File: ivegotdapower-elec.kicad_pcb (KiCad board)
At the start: 2 copper layers, 87 x 70 mm, 74 parts, among them J1 Conn_Debug, J10 Conn_+3.3V, J11 Conn_bau, J12 CAN_conn, J13 CAN_conn, J2 Conn_batt, J3 Conn_alim, J4 Conn_TSMR, J5 Conn_POW2, J6 Conn_POW1, J7 Conn_RPi, J8 Conn_+5V, Q1 IRFR5305, Q2 IRFR5305, Q3 BSS138, Q4 MMBT2907A, Q5 MMBT2907A, Q6 MMBT2907A, Q7 MMBT2907A, U1 TCAN332, U10 LD1117S33TR_SOT223, U11 LM358, U6 ACS711xLCTR-12AB, U7 STM32F303K8Tx, U8 LD1117S50TR_SOT223

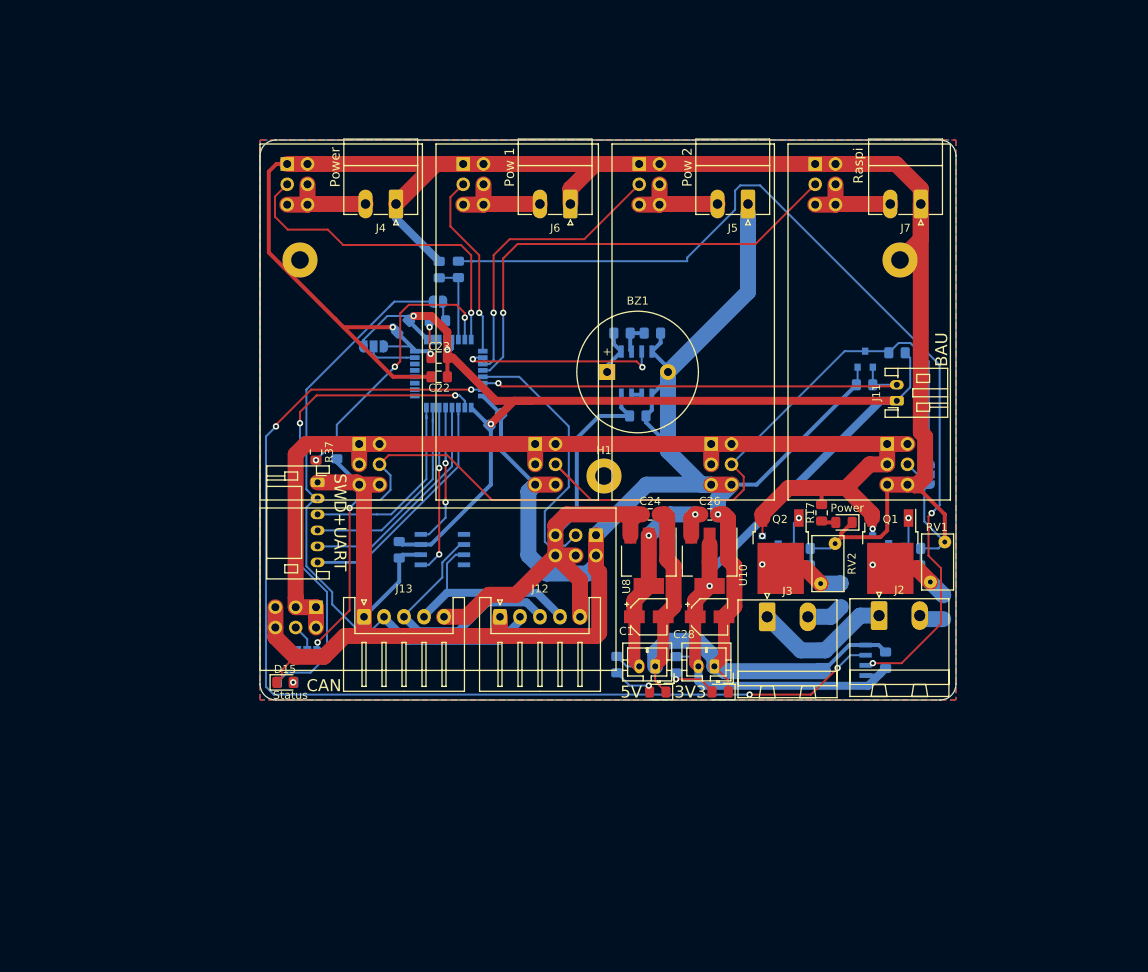
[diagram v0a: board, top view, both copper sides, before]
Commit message: Refactoring. Add protection (OpAmps) on analog measures
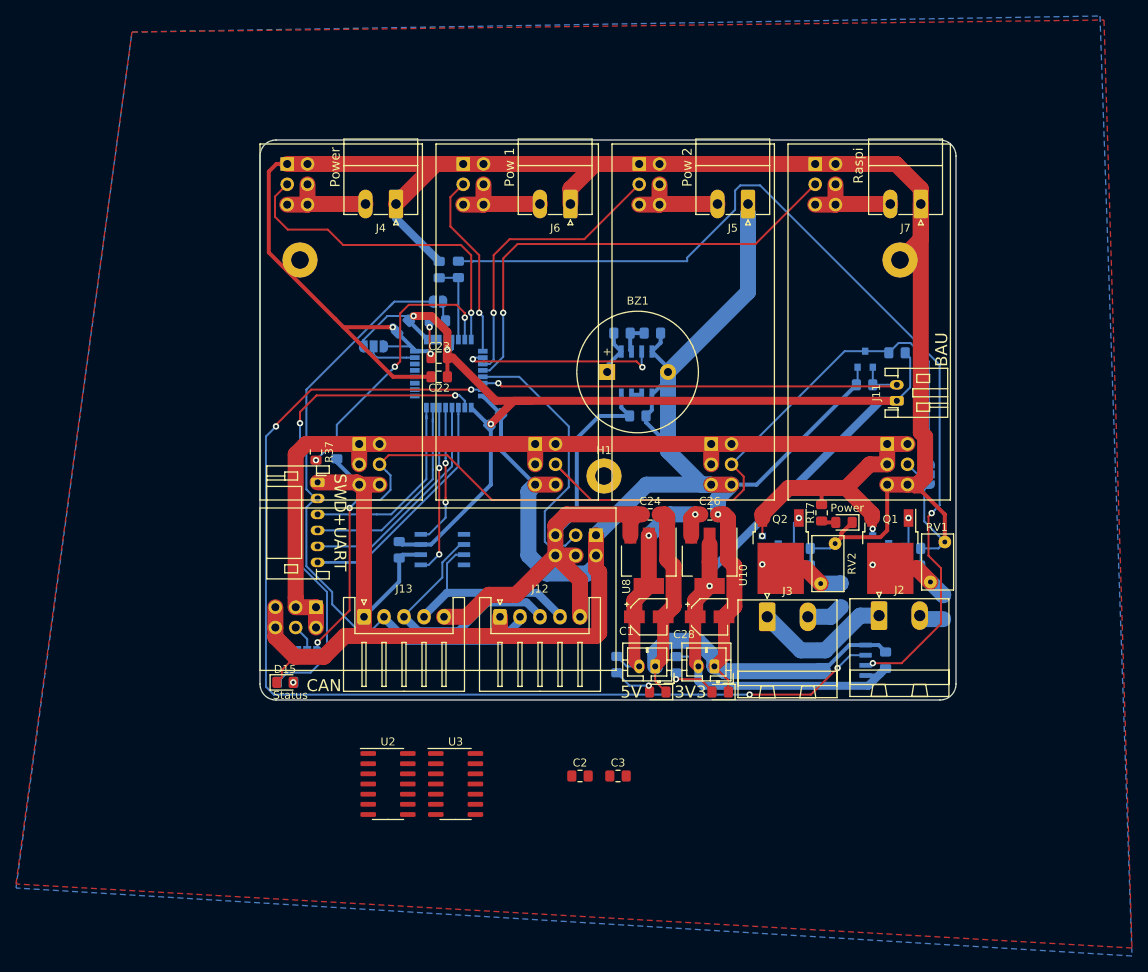
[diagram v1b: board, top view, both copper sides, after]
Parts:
- added C2: 100nF, Capacitor_SMD:C_0805_2012Metric_Pad1.15x1.40mm_HandSolder, F.Cu at (120.0, 129.5)
- added C3: 100nF, Capacitor_SMD:C_0805_2012Metric_Pad1.15x1.40mm_HandSolder, F.Cu at (124.8, 129.5)
- added U2: LM324, Package_SO:SOIC-14_3.9x8.7mm_P1.27mm, F.Cu at (96.0, 130.5)
- added U3: LM324, Package_SO:SOIC-14_3.9x8.7mm_P1.27mm, F.Cu at (104.5, 130.5)
- R37: value R -> 75k
- R38: value R -> 15k
- U10: value LD1117S33TR_SOT223 -> LD1117S33TR
- U8: value LD1117S50TR_SOT223 -> LD1117S50TR
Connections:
- net /STM32/nrst renamed /STM32/rst
- net Net-(C1-Pad1) renamed +5V
- net Net-(U11-Pad3) renamed /STM32/Buzzer
- B5 pad 9: /STM32/TSMR -> /buck/TSMR_mes
- C16 pad 1: +7.5V -> GND
- C16 pad 2: GND -> +7.5V
- R37 pad 2: /STM32/raw -> /STM32/mes_raw
- R38 pad 1: /STM32/raw -> /STM32/mes_raw
- R42 pad 1: Net-(BZ1-Pad1) -> Net-(R41-Pad2)
- R42 pad 2: Net-(R41-Pad2) -> Net-(BZ1-Pad1)
- U1 pad 5: Net-(U1-Pad5) -> (no net)
- U1 pad 8: Net-(U1-Pad8) -> (no net)
- U7 pad 11: /buck/Pow2_mes -> /STM32/mes_protected_pow2
- U7 pad 12: /buck/RPi_mes -> /STM32/mes_protected_rpi
- U7 pad 13: /buck/Logic_mes -> /STM32/mes_protected_logic
- U7 pad 2: Net-(U7-Pad2) -> (no net)
- U7 pad 25: Net-(U7-Pad25) -> (no net)
- U7 pad 26: Net-(U7-Pad26) -> (no net)
- U7 pad 27: Net-(U7-Pad27) -> (no net)
- U7 pad 28: Net-(U7-Pad28) -> (no net)
- U7 pad 29: Net-(U7-Pad29) -> (no net)
- U7 pad 3: Net-(U7-Pad3) -> (no net)
- U7 pad 30: Net-(U7-Pad30) -> (no net)
- U7 pad 7: /STM32/raw -> /STM32/mes_protected_raw
- U7 pad 8: /STM32/TSMR -> /STM32/mes_protected_TSMR
- U7 pad 9: /buck/Pow1_mes -> /STM32/mes_protected_pow1
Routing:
- net (no net): track 0.00 -> 193.4 mm, vias 0 -> 4
- net /buck/RPi_mes: track 58.4 -> 0.00 mm, vias 1 -> 0
- net /STM32/TSMR: track 41.8 -> 0.00 mm, vias 1 -> 0
- net /buck/Pow2_mes: track 36.5 -> 0.00 mm, vias 1 -> 0
- net /buck/Logic_mes: track 33.6 -> 0.00 mm
- net /buck/Pow1_mes: track 23.2 -> 0.00 mm, vias 1 -> 0

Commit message: Fix libs
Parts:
- removed D15: LED, LED_SMD:LED_0805_2012Metric_Pad1.15x1.40mm_HandSolder
- removed JP1: Jumper_NC_Small, Jumper:SolderJumper-2_P1.3mm_Open_RoundedPad1.0x1.5mm
- removed R24: R, Resistor_SMD:R_0805_2012Metric_Pad1.15x1.40mm_HandSolder
- added D2: LED_ARGB, LED_SMD:LED_Cree-PLCC4_2x2mm_CW, F.Cu at (140.0, 135.8)
- added Q10: BSS138, Package_TO_SOT_SMD:SOT-23, F.Cu at (141.1, 129.6)
- added Q11: BSS138, Package_TO_SOT_SMD:SOT-23, F.Cu at (145.5, 129.6)
- added Q8: BSS138, Package_TO_SOT_SMD:SOT-23, F.Cu at (136.6, 129.6)
- added Q9: BSS138, Package_TO_SOT_SMD:SOT-23, F.Cu at (136.6, 134.2)
- added R2: 91, Resistor_SMD:R_0805_2012Metric_Pad1.15x1.40mm_HandSolder, F.Cu at (157.3, 128.8)
- added R3: 27, Resistor_SMD:R_0805_2012Metric_Pad1.15x1.40mm_HandSolder, F.Cu at (157.3, 131.8)
- added R4: 39, Resistor_SMD:R_0805_2012Metric_Pad1.15x1.40mm_HandSolder, F.Cu at (162.1, 128.8)
- added R5: 10k, Resistor_SMD:R_0805_2012Metric_Pad1.15x1.40mm_HandSolder, F.Cu at (122.3, 135.3)
- added R6: 10k, Resistor_SMD:R_0805_2012Metric_Pad1.15x1.40mm_HandSolder, F.Cu at (122.3, 138.3)
- added R7: 10k, Resistor_SMD:R_0805_2012Metric_Pad1.15x1.40mm_HandSolder, F.Cu at (127.0, 135.3)
- added R8: 10k, Resistor_SMD:R_0805_2012Metric_Pad1.15x1.40mm_HandSolder, F.Cu at (127.0, 138.3)
- added R9: 10k, Resistor_SMD:R_0805_2012Metric_Pad1.15x1.40mm_HandSolder, F.Cu at (131.8, 135.3)
- turned C16 to 180 degrees
- turned R42 to 180 degrees
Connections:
- net /STM32/sense renamed /STM32/mes_current
- net /STM32/sense_fault renamed /STM32/mes_current_fault
- net /buck/on-off renamed /buck/~on~-off
- net /buck/power renamed IN
- net Net-(C19-Pad1) renamed /STM32/reset_logic/Reset_MCU
- J1 pad 2: /STM32/rst -> /STM32/reset_swd
- J12 pad 2: /STM32/rst -> /STM32/reset_can
- J13 pad 2: /STM32/rst -> /STM32/reset_can
- U1 pad 5: (no net) -> Net-(U1-Pad5)
- U1 pad 8: (no net) -> Net-(U1-Pad8)
- U7 pad 2: (no net) -> Net-(U7-Pad2)
- U7 pad 25: (no net) -> Net-(U7-Pad25)
- U7 pad 26: (no net) -> Net-(U7-Pad26)
- U7 pad 27: (no net) -> Net-(U7-Pad27)
- U7 pad 28: (no net) -> Net-(R2-Pad1)
- U7 pad 29: (no net) -> Net-(R3-Pad1)
- U7 pad 3: (no net) -> Net-(U7-Pad3)
- U7 pad 30: (no net) -> Net-(R4-Pad1)
